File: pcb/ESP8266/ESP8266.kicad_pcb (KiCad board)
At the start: 2 copper layers, 18 parts, among them J1 Conn_02x04, U1 ESP8266EX, U2 W25Q16BVSSIG

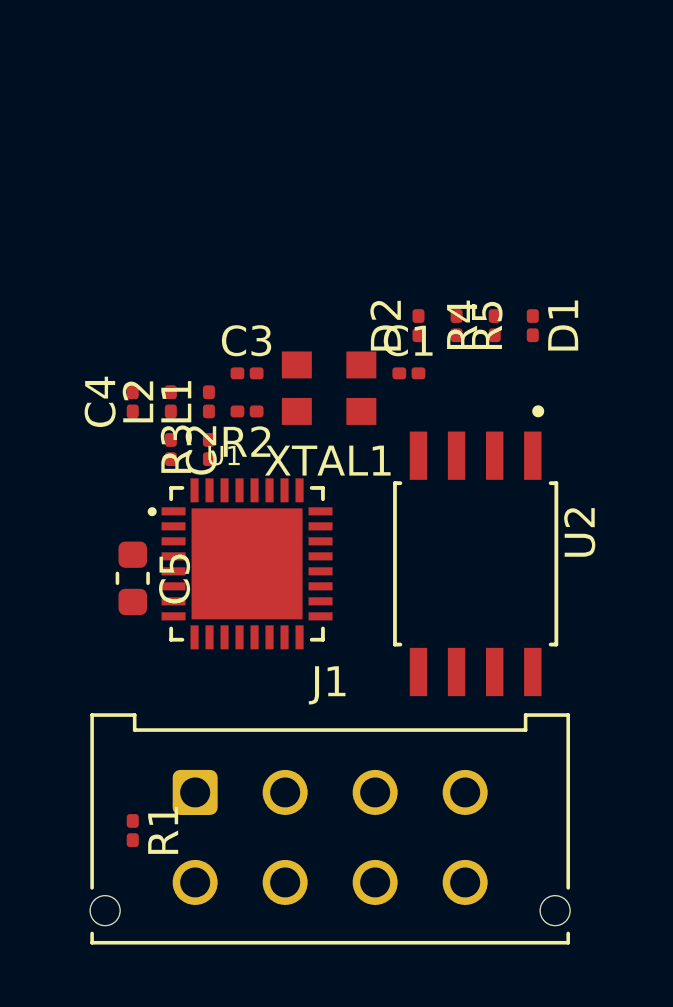
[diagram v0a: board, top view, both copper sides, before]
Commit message: modificacion linea esquematico, avances en pcb
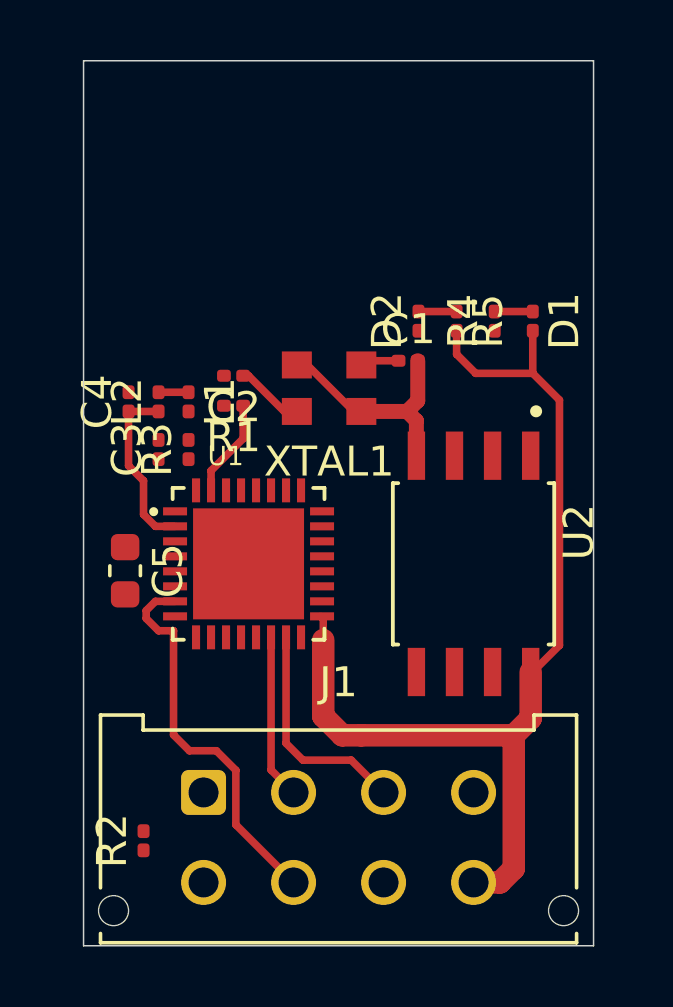
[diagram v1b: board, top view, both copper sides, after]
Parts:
- moved R2 14.7 mm to (104.5, 137.5), turned to 90 degrees
- moved R1 14.6 mm to (107.5, 123.0), turned to 180 degrees
- moved C3 3.89 mm to (105.0, 124.5), turned to 90 degrees
- moved C2 3.23 mm to (107.5, 122.0), turned to 180 degrees
- moved L1 0.68 mm to (106.0, 122.9), turned to 270 degrees
- moved R3 0.68 mm to (106.0, 124.5)
- moved C1 0.42 mm to (113.3, 121.5)
- moved L2 0.41 mm to (105.0, 122.9)
- moved C5 0.36 mm to (103.9, 128.5)
- moved J1 0.28 mm to (106.5, 135.9)
- moved D1 0.15 mm to (117.5, 120.2)
- moved D2 0.15 mm to (113.7, 120.2)
- moved R4 0.15 mm to (116.2, 120.2)
- moved R5 0.15 mm to (114.9, 120.2)
- moved C4 0.14 mm to (104.0, 122.9)
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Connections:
- U1 pad 22: Net-(U1-Pad22) -> /SD0
- U2 pad 2: Net-(U1-Pad23) -> /SD0
- U2 pad 5: Net-(U1-Pad22) -> Net-(U1-Pad23)
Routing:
- net +3V3: track 0.00 -> 34.0 mm
- net /ENA: track 0.00 -> 13.0 mm
- net GND: track 0.00 -> 8.76 mm
- net /GPIO0: track 0.00 -> 7.46 mm
- net Net-(C4-Pad1): track 0.00 -> 5.86 mm
- net /GPIO2: track 0.00 -> 5.48 mm
- net Net-(R1-Pad1): track 0.00 -> 3.26 mm
- net /SA_XTAL: track 0.00 -> 2.38 mm
- net /EN_XTAL: track 0.00 -> 1.30 mm
- net Net-(D2-Pad2): track 0.00 -> 1.27 mm
- net Net-(D1-Pad1): track 0.00 -> 1.27 mm
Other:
- board outline added: 17 x 29.5 mm

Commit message: cambio de footprint en las resistencias y capacitores, fin de pcb V1.0
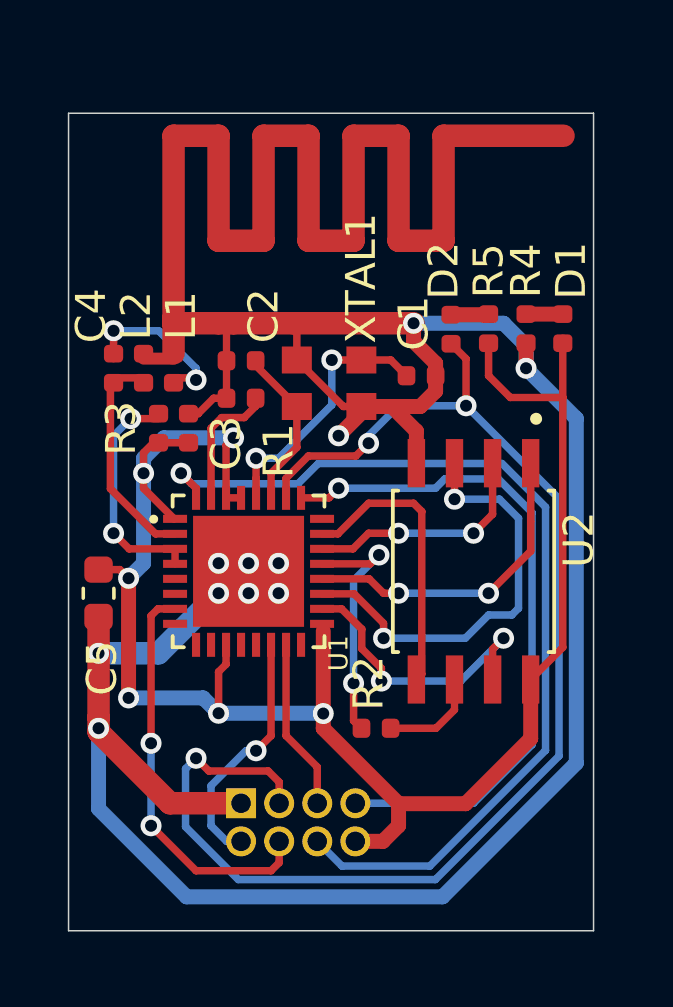
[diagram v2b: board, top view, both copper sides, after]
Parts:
- C1, C2, C3, C4: footprint Capacitor_SMD:C_0201_0603Metric -> Capacitor_SMD:C_0402_1005Metric
- D1, D2, R1, R2, R3, R4, R5: footprint Resistor_SMD:R_0201_0603Metric -> Resistor_SMD:R_0402_1005Metric
- J1: footprint Connector_Molex:Molex_Micro-Fit_3.0_43045-0812_2x04_P3.00mm_Vertical -> Connector_PinHeader_1.27mm:PinHeader_2x04_P1.27mm_Vertical; moved to B.Cu
- L1, L2: footprint Inductor_SMD:L_0201_0603Metric -> Inductor_SMD:L_0402_1005Metric
- moved R2 8.61 mm to (112.2, 133.8), turned to 180 degrees
- moved J1 1.30 mm to (107.8, 136.2), turned to 270 degrees
- moved C4 1.23 mm to (103.5, 121.8)
- moved L1 1.23 mm to (105.5, 121.8)
- moved L2 1.23 mm to (104.5, 121.8)
- moved C3 1.23 mm to (106.0, 123.8)
- moved R3 1.23 mm to (105.0, 123.8)
- moved C5 1.16 mm to (103.0, 129.2)
- moved D2 1.12 mm to (114.8, 120.5)
- moved R5 1.09 mm to (116.0, 120.4)
- moved R4 1.07 mm to (117.2, 120.4)
- moved D1 1.03 mm to (118.5, 120.4)
- moved C1 0.66 mm to (113.8, 122.0)
- moved C2 0.56 mm to (107.8, 121.5)
- moved R1 0.35 mm to (107.8, 122.8)
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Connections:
- J1 pad 3: /GPIO0 -> /UTXD
- J1 pad 4: /URXD -> /ENA
- J1 pad 5: /UTXD -> /GPIO0
- J1 pad 6: /ENA -> /RST
- J1 pad 7: /RST -> /URXD
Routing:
- net GND: track 8.76 -> 128.9 mm, vias 0 -> 11
- net /UTXD: track 0.00 -> 44.2 mm, vias 0 -> 3
- net /RST: track 0.00 -> 31.9 mm, vias 0 -> 1
- net +3V3: track 34.0 -> 60.6 mm, vias 0 -> 6
- net /URXD: track 0.00 -> 22.9 mm, vias 0 -> 1
- net Net-(U1-Pad19): track 0.00 -> 14.5 mm, vias 0 -> 2
- net Net-(U1-Pad20): track 0.00 -> 10.7 mm, vias 0 -> 2
- net Net-(U1-Pad18): track 0.00 -> 9.80 mm, vias 0 -> 2
- net Net-(U1-Pad23): track 0.00 -> 9.54 mm
- net Net-(R2-Pad2): track 0.00 -> 8.26 mm, vias 0 -> 2
- net /SD0: track 0.00 -> 7.86 mm, vias 0 -> 2
- net Net-(R3-Pad2): track 0.00 -> 7.75 mm, vias 0 -> 2
- net /EN_XTAL: track 1.30 -> 8.79 mm, vias 0 -> 2
- net Net-(C4-Pad2): track 0.00 -> 5.37 mm, vias 0 -> 2
- net Net-(R2-Pad1): track 0.00 -> 3.39 mm
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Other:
- board size 17 x 29.5 mm -> 17.5 x 27.2 mm
